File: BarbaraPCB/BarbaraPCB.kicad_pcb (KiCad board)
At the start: 2 copper layers, 195.3 x 125.5 mm, 147 parts, among them J1 Conn_01x05_Pin, J2 Conn_01x05_Pin, J3 Conn_01x05_Pin_reversed, J4 Conn_01x05_Pin_reversed, SW1 SW_Push, SW10 SW_Push, SW11 SW_Push, SW12 SW_Push, SW13 SW_Push, SW14 SW_Push, SW15 SW_Push, SW16 SW_Push, SW17 SW_Push, SW18 SW_Push, SW19 SW_Push, SW2 SW_Push, SW20 SW_Push, SW21 SW_Push_1.5u, SW22 SW_Push, SW23 SW_Push, SW24 SW_Push, SW25 SW_Push, SW26 SW_Push, SW27 SW_Push, SW28 SW_Push, SW29 SW_Push_1.5u, SW3 SW_Push, SW30 SW_Push, SW31 SW_Push, SW32 SW_Push, SW33 SW_Push, SW34 SW_Push, SW35 SW_Push_1.25u, SW36 SW_Push_1.75u, SW37 SW_Push_1.75u, SW38 SW_Push_1.25u, SW39 SW_Push, SW4 SW_Push, SW40 SW_Push, SW41 SW_Push, SW42 SW_Push, SW43 SW_Push, SW44 SW_Push, SW45 SW_Push_1.5u, SW46 SW_Push_1.5u, SW47 SW_Push_1.5u, SW48 SW_Push_1.5u, SW49 SW_Push, SW5 SW_Push, SW50 SW_Push, SW51 SW_Push, SW52 SW_Push, SW53 SW_Push, SW54 SW_Push_1.25u, SW55 SW_Push_1.75u, SW56 SW_Push_1.75u, SW57 SW_Push_1.25u, SW58 SW_Push, SW59 SW_Push, SW6 SW_Push, SW60 SW_Push, SW61 SW_Push, SW62 SW_Push, SW63 SW_Push, SW64 SW_Push_1.5u, SW65 SW_Push_1.5u, SW66 SW_Push_1.5u, SW67 SW_Push_1.5u, SW7 SW_Push, SW8 SW_Push, SW9 SW_Push, U1 RP2040-Matrix

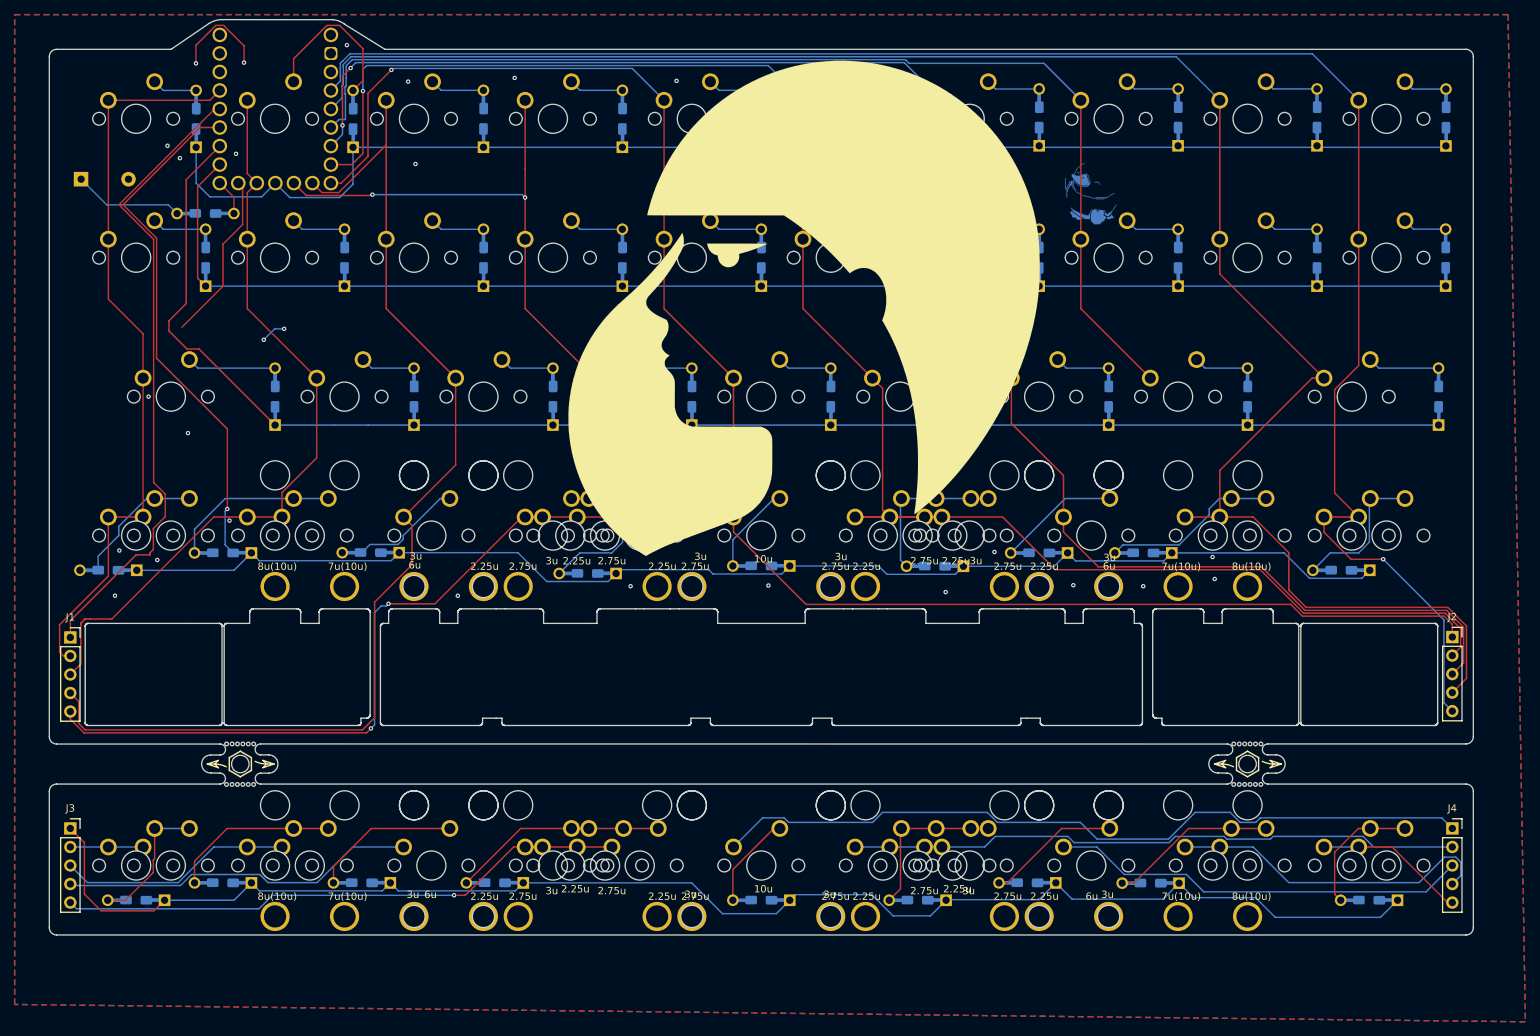
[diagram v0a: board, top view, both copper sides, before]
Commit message: Removed the thin parts in the plate part of the PCB, were too small for manufacturing. Ordered first Protos.
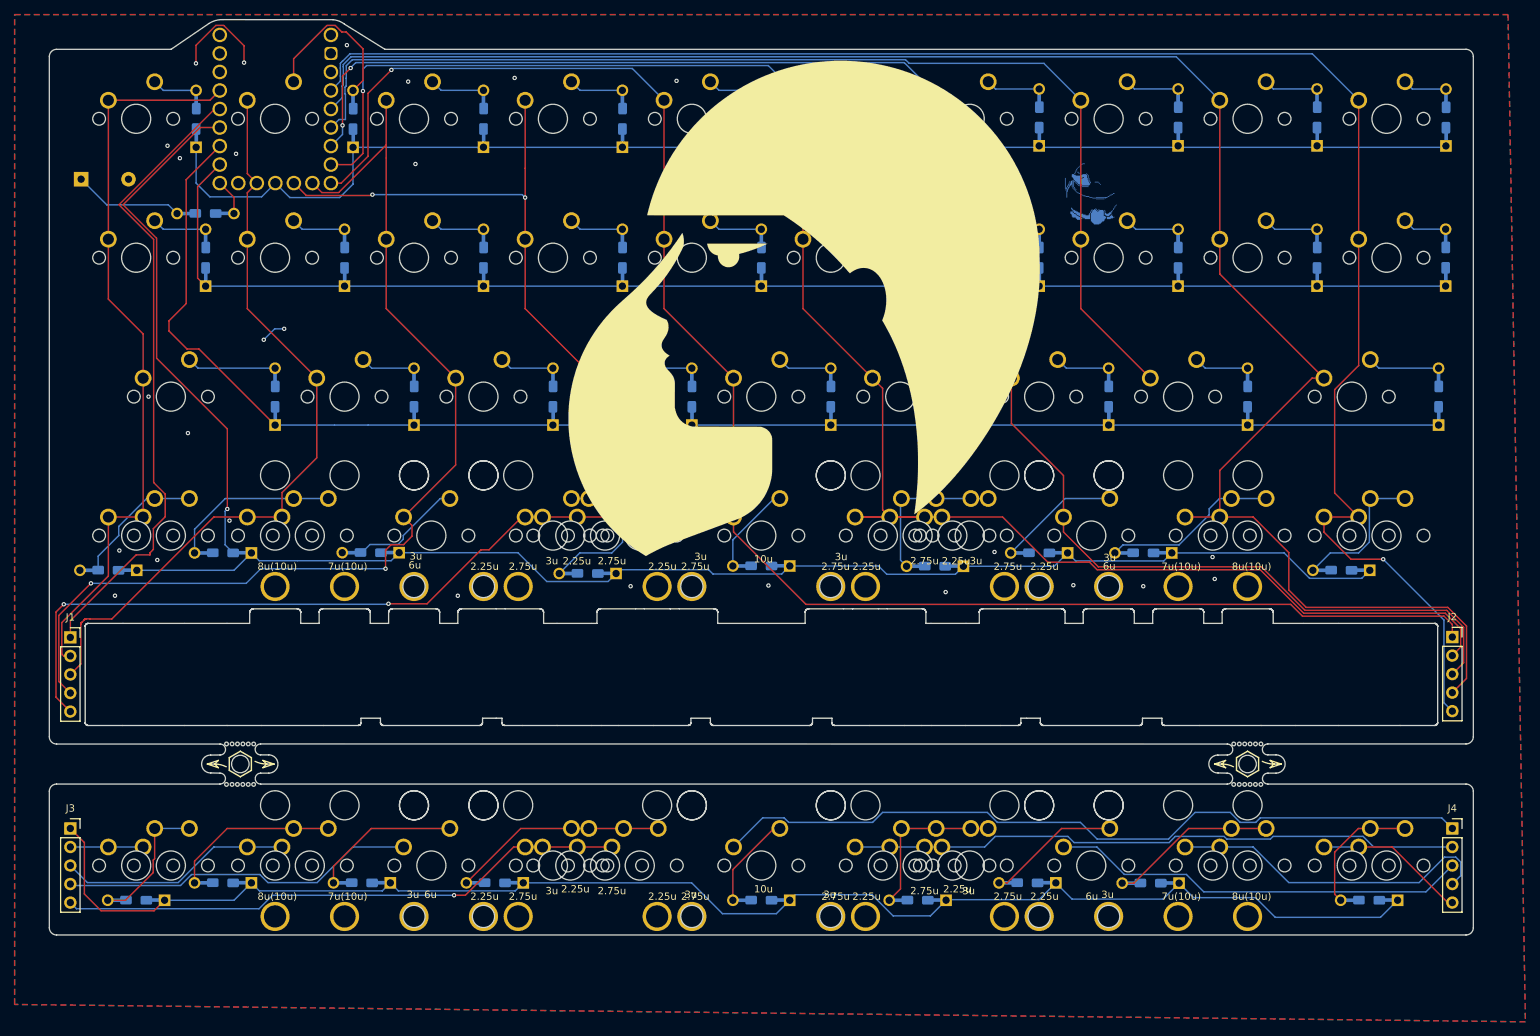
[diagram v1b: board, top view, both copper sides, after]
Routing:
- net unconnected-(U1-P9-Pad23): track 23.4 -> 0.00 mm
- net row2: track 153.8 -> 146.2 mm, vias 0 -> 2
- net row3: track 192.1 -> 190.8 mm
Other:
- outline, holes or cut-outs redrawn
